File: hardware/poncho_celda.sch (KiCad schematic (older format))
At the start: 0 parts

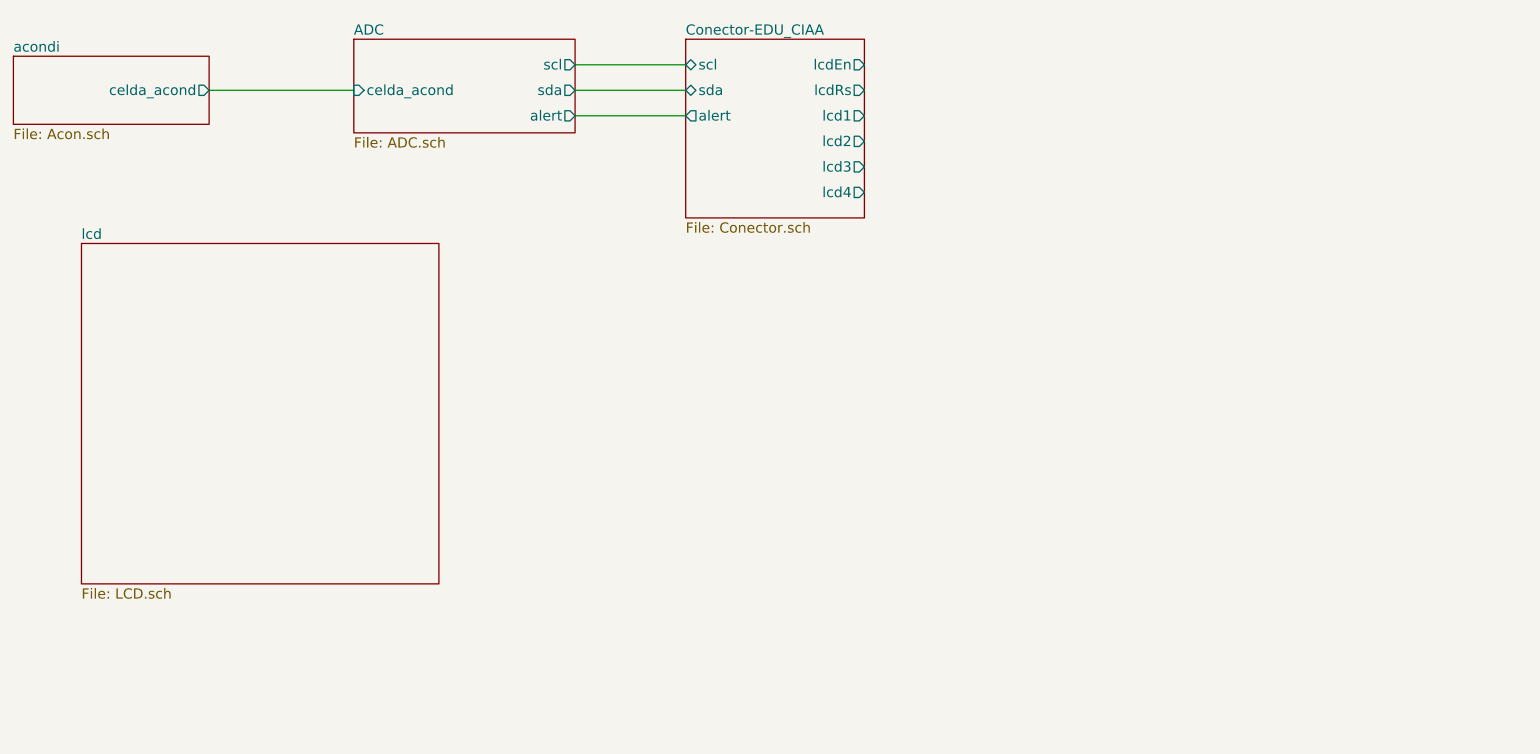
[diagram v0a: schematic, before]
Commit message: Se finalizo esquematico del cricuito.
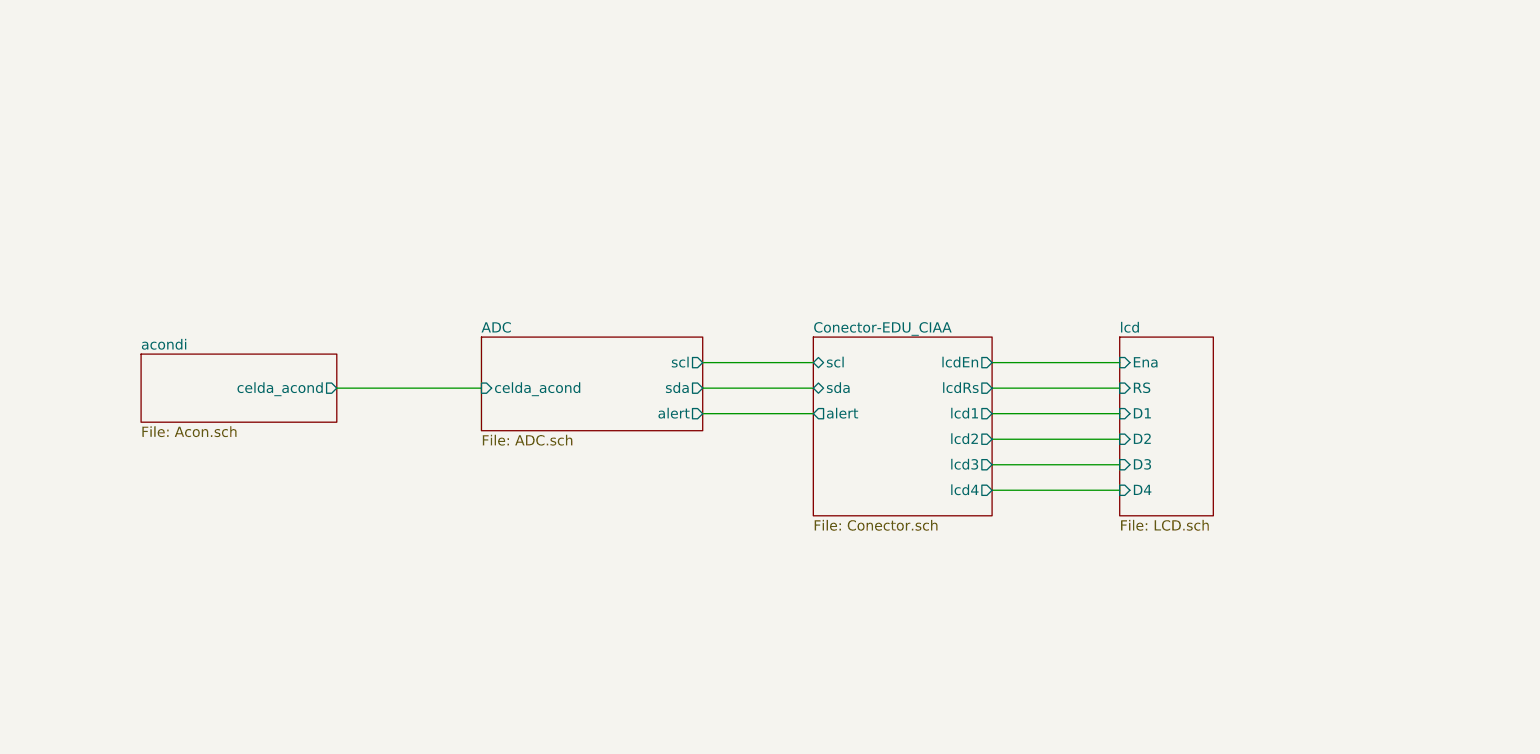
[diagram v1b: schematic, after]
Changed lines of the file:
@@
 encoding utf-8
 Sheet 1 5
-Title ""
-Date ""
+Title "Diagrama esquematico de modulos para poncho celda."
+Date "2016-07-04"
 Rev ""
-Comp ""
+Comp "Felipe Rey"
 Comment1 ""
 Comment2 ""
@@
 $EndDescr
 $Sheet
-S 3600 1500 1300 550
+S 4350 3250 1300 550
 U 57856888
 F0 "ADC" 60
 F1 "ADC.sch" 60
-F2 "celda_acond" I L 3600 1800 60
-F3 "scl" O R 4900 1650 60
-F4 "sda" O R 4900 1800 60
-F5 "alert" O R 4900 1950 60
+F2 "celda_acond" I L 4350 3550 60
+F3 "scl" O R 5650 3400 60
+F4 "sda" O R 5650 3550 60
+F5 "alert" O R 5650 3700 60
 $EndSheet
 $Sheet
-S 1600 1600 1150 400
+S 2350 3350 1150 400
 U 578568AB
 F0 "acondi" 60
 F1 "Acon.sch" 60
-F2 "celda_acond" O R 2750 1800 60
+F2 "celda_acond" O R 3500 3550 60
 $EndSheet
 $Sheet
-S 2000 2700 2100 2000
+S 8100 3250 550  1050
 U 578568C8
 F0 "lcd" 60
 F1 "LCD.sch" 60
+F2 "RS" I L 8100 3550 60
+F3 "Ena" I L 8100 3400 60
+F4 "D1" I L 8100 3700 60
+F5 "D2" I L 8100 3850 60
+F6 "D3" I L 8100 4000 60
+F7 "D4" I L 8100 4150 60
 $EndSheet
 $Sheet
-S 5550 1500 1050 1050
+S 6300 3250 1050 1050
 U 578568DA
 F0 "Conector-EDU_CIAA" 60
 F1 "Conector.sch" 60
-F2 "sda" B L 5550 1800 60
-F3 "scl" B L 5550 1650 60
-F4 "lcdEn" O R 6600 1650 60
-F5 "lcdRs" O R 6600 1800 60
-F6 "lcd1" O R 6600 1950 60
-F7 "lcd2" O R 6600 2100 60
-F8 "lcd3" O R 6600 2250 60
-F9 "lcd4" O R 6600 2400 60
-F10 "alert" O L 5550 1950 60
+F2 "sda" B L 6300 3550 60
+F3 "scl" B L 6300 3400 60
+F4 "lcdEn" O R 7350 3400 60
+F5 "lcdRs" O R 7350 3550 60
+F6 "lcd1" O R 7350 3700 60
+F7 "lcd2" O R 7350 3850 60
+F8 "lcd3" O R 7350 4000 60
+F9 "lcd4" O R 7350 4150 60
+F10 "alert" O L 6300 3700 60
 $EndSheet
 Wire Wire Line
-	2750 1800 3600 1800
+	3500 3550 4350 3550
 Wire Wire Line
-	4900 1650 5550 1650
+	5650 3400 6300 3400
 Wire Wire Line
-	4900 1800 5550 1800
+	5650 3550 6300 3550
 Wire Wire Line
-	4900 1950 5550 1950
+	5650 3700 6300 3700
+Wire Wire Line
+	7350 3400 8100 3400
+Wire Wire Line
+	8100 3550 7350 3550
+Wire Wire Line
+	8100 3700 7350 3700
+Wire Wire Line
+	8100 3850 7350 3850
+Wire Wire Line
+	8100 4000 7350 4000
+Wire Wire Line
+	8100 4150 7350 4150
 $EndSCHEMATC

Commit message: Se realizan correcciones al esquematico.
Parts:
- added DS1: LCD16X2, celda:LCD16x2, symbol LCD16X2
- added R7: 220, celda:R_1206_HandSoldering, symbol R
- added RV1: 10K, celda:POT_SMD, symbol POT
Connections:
- net Conector-EDU_CIAA/lcd1: now also DS1.11 (D4)
- net Conector-EDU_CIAA/lcd2: now also DS1.12 (D5)
- net Conector-EDU_CIAA/lcd3: now also DS1.13 (D6)
- net Conector-EDU_CIAA/lcd4: now also DS1.14 (D7)
- net Conector-EDU_CIAA/lcdEn: now also DS1.6 (E)
- net Conector-EDU_CIAA/lcdRs: now also DS1.4 (RS)
- new net: DS1.16 (LED-), R7.1
- new net: DS1.3 (VO), RV1.2
- new net +5V: DS1.15 (LED+), DS1.2 (VDD), RV1.1
- new net GND: DS1.1 (VSS), DS1.10 (D3), DS1.5 (R/W), DS1.7 (D0), DS1.8 (D1), DS1.9 (D2), R7.2, RV1.3
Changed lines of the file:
@@
 $Descr A4 11693 8268
 encoding utf-8
-Sheet 1 5
-Title "Diagrama esquematico de modulos para poncho celda."
+Sheet 1 3
+Title "Diagrama esquematico de poncho Celda."
 Date "2016-07-04"
 Rev ""
 Comp "Felipe Rey"
-Comment1 ""
-Comment2 ""
+Comment1 "Diagrama esquematico de modulos para poncho celda para el curso de Diseño de PCB del CESE."
+Comment2 "Licencia GPL V3"
 Comment3 ""
 Comment4 ""
 $EndDescr
 $Sheet
-S 4350 3250 1300 550
-U 57856888
-F0 "ADC" 60
-F1 "ADC.sch" 60
-F2 "celda_acond" I L 4350 3550 60
-F3 "scl" O R 5650 3400 60
-F4 "sda" O R 5650 3550 60
-F5 "alert" O R 5650 3700 60
+S 3000 4500 950  600
+U 578568AB
+F0 "Adqui_Celda" 60
+F1 "Acon.sch" 60
+F2 "scl" O R 3950 4600 60
+F3 "sda" O R 3950 4750 60
+F4 "alert" O R 3950 4900 60
 $EndSheet
 $Sheet
-S 2350 3350 1150 400
-U 578568AB
-F0 "acondi" 60
-F1 "Acon.sch" 60
-F2 "celda_acond" O R 3500 3550 60
-$EndSheet
-$Sheet
-S 8100 3250 550  1050
-U 578568C8
-F0 "lcd" 60
-F1 "LCD.sch" 60
-F2 "RS" I L 8100 3550 60
-F3 "Ena" I L 8100 3400 60
-F4 "D1" I L 8100 3700 60
-F5 "D2" I L 8100 3850 60
-F6 "D3" I L 8100 4000 60
-F7 "D4" I L 8100 4150 60
-$EndSheet
-$Sheet
-S 6300 3250 1050 1050
+S 4600 4450 1050 1050
 U 578568DA
 F0 "Conector-EDU_CIAA" 60
 F1 "Conector.sch" 60
-F2 "sda" B L 6300 3550 60
-F3 "scl" B L 6300 3400 60
-F4 "lcdEn" O R 7350 3400 60
-F5 "lcdRs" O R 7350 3550 60
-F6 "lcd1" O R 7350 3700 60
-F7 "lcd2" O R 7350 3850 60
-F8 "lcd3" O R 7350 4000 60
-F9 "lcd4" O R 7350 4150 60
-F10 "alert" O L 6300 3700 60
+F2 "sda" B L 4600 4750 60
+F3 "scl" B L 4600 4600 60
+F4 "lcdEn" O R 5650 4750 60
+F5 "lcdRs" O R 5650 4600 60
+F6 "lcd1" O R 5650 4900 60
+F7 "lcd2" O R 5650 5050 60
+F8 "lcd3" O R 5650 5200 60
+F9 "lcd4" O R 5650 5350 60
+F10 "alert" O L 4600 4900 60
 $EndSheet
 Wire Wire Line
-	3500 3550 4350 3550
+	3950 4600 4600 4600
 Wire Wire Line
-	5650 3400 6300 3400
+	3950 4750 4600 4750
 Wire Wire Line
-	5650 3550 6300 3550
+	3950 4900 4600 4900
+$Comp
+L LCD16X2 DS1
+U 1 1 5796E83B
+P 6600 1800
+F 0 "DS1" H 5800 2200 50  0000 C CNN
+F 1 "LCD16X2" H 7300 2200 50  0000 C CNN
+F 2 "celda:LCD16x2" H 6600 1750 50  0000 C CIN
+F 3 "" H 6600 1800 50  0000 C CNN
+	1    6600 1800
+	1    0    0    -1
+$EndComp
+$Comp
+L POT RV1
+U 1 1 5796E97F
+P 5100 2850
+F 0 "RV1" H 5100 2750 50  0000 C CNN
+F 1 "10K" H 5100 2850 50  0000 C CNN
+F 2 "celda:POT_SMD" H 5100 2850 50  0001 C CNN
+F 3 "" H 5100 2850 50  0000 C CNN
+	1    5100 2850
+	0    1    1    0
+$EndComp
+$Comp
+L +5V #PWR01
+U 1 1 5796F4BD
+P 5100 2200
+F 0 "#PWR01" H 5100 2050 50  0001 C CNN
+F 1 "+5V" H 5100 2340 50  0000 C CNN
+F 2 "" H 5100 2200 50  0000 C CNN
+F 3 "" H 5100 2200 50  0000 C CNN
+	1    5100 2200
+	1    0    0    -1
+$EndComp
+$Comp
+L +5V #PWR02
+U 1 1 5796F541
+P 7750 2150
+F 0 "#PWR02" H 7750 2000 50  0001 C CNN
+F 1 "+5V" H 7750 2290 50  0000 C CNN
+F 2 "" H 7750 2150 50  0000 C CNN
+F 3 "" H 7750 2150 50  0000 C CNN
+	1    7750 2150
+	1    0    0    -1
+$EndComp
+$Comp
+L R R7
+U 1 1 5796F5C5
+P 7350 2750
+F 0 "R7" V 7430 2750 50  0000 C CNN
+F 1 "220" V 7350 2750 50  0000 C CNN
+F 2 "celda:R_1206_HandSoldering" V 7280 2750 50  0001 C CNN
+F 3 "" H 7350 2750 50  0000 C CNN
+	1    7350 2750
+	1    0    0    -1
+$EndComp
 Wire Wire Line
-	5650 3700 6300 3700
+	7350 2300 7350 2600
 Wire Wire Line
-	7350 3400 8100 3400
+	7250 2300 7250 2450
 Wire Wire Line
-	8100 3550 7350 3550
+	7250 2450 7750 2450
 Wire Wire Line
-	8100 3700 7350 3700
+	7750 2450 7750 2150
 Wire Wire Line
-	8100 3850 7350 3850
+	5950 2300 5950 2450
 Wire Wire Line
-	8100 4000 7350 4000
+	5950 2450 5100 2450
 Wire Wire Line
-	8100 4150 7350 4150
+	5100 2200 5100 2600
+Connection ~ 5100 2450
+Wire Wire Line
+	6050 2300 6050 2850
+Wire Wire Line
+	6050 2850 5250 2850
+$Comp
+L GND #PWR03
+U 1 1 5796F813
+P 5850 3400
+F 0 "#PWR03" H 5850 3150 50  0001 C CNN
+F 1 "GND" H 5850 3250 50  0000 C CNN
+F 2 "" H 5850 3400 50  0000 C CNN
+F 3 "" H 5850 3400 50  0000 C CNN
+	1    5850 3400
+	1    0    0    -1
+$EndComp
+$Comp
+L GND #PWR04
+U 1 1 5796F899
+P 7350 3350
+F 0 "#PWR04" H 7350 3100 50  0001 C CNN
+F 1 "GND" H 7350 3200 50  0000 C CNN
+F 2 "" H 7350 3350 50  0000 C CNN
+F 3 "" H 7350 3350 50  0000 C CNN
+	1    7350 3350
+	1    0    0    -1
+$EndComp
+Wire Wire Line
+	7350 2900 7350 3350
+Wire Wire Line
+	5850 2300 5850 3400
+Wire Wire Line
+	5100 3100 5100 3300
+Wire Wire Line
+	5100 3300 5850 3300
+Connection ~ 5850 3300
+Wire Wire Line
+	6250 2300 6250 2600
+Wire Wire Line
+	5850 2600 6750 2600
+Connection ~ 5850 2600
+Wire Wire Line
+	6450 2600 6450 2300
+Connection ~ 6250 2600
+Wire Wire Line
+	6550 2600 6550 2300
+Connection ~ 6450 2600
+Wire Wire Line
+	6650 2600 6650 2300
+Connection ~ 6550 2600
+Wire Wire Line
+	6750 2600 6750 2300
+Connection ~ 6650 2600
+Wire Wire Line
+	5650 4600 6150 4600
+Wire Wire Line
+	6150 4600 6150 2300
+Wire Wire Line
+	5650 4750 6350 4750
+Wire Wire Line
+	6350 4750 6350 2300
+Wire Wire Line
+	5650 4900 6850 4900
+Wire Wire Line
+	6850 4900 6850 2300
+Wire Wire Line
+	5650 5050 6950 5050
+Wire Wire Line
+	6950 5050 6950 2300
+Wire Wire Line
+	5650 5200 7050 5200
+Wire Wire Line
+	7050 5200 7050 2300
+Wire Wire Line
+	5650 5350 7150 5350
+Wire Wire Line
+	7150 5350 7150 2300
 $EndSCHEMATC

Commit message: Correcciones en clases.
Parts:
- added F1, F2, F3: FIDUCIAL, celda:Fiducial_1mm, symbol FIDUCIAL
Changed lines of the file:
@@
 EESchema Schematic File Version 2
-LIBS:power
-LIBS:device
-LIBS:transistors
-LIBS:conn
-LIBS:linear
-LIBS:regul
-LIBS:74xx
-LIBS:cmos4000
-LIBS:adc-dac
-LIBS:memory
-LIBS:xilinx
-LIBS:microcontrollers
-LIBS:dsp
-LIBS:microchip
-LIBS:analog_switches
-LIBS:motorola
-LIBS:texas
-LIBS:intel
-LIBS:audio
-LIBS:interface
-LIBS:digital-audio
-LIBS:philips
-LIBS:display
-LIBS:cypress
-LIBS:siliconi
-LIBS:opto
-LIBS:atmel
-LIBS:contrib
-LIBS:valves
 LIBS:ej2cese
-LIBS:ADS1113IDGSR
 LIBS:poncho_celda-cache
 EELAYER 25 0
@@
 Rev ""
 Comp "Felipe Rey Hernandez"
-Comment1 "Diagrama esquematico de modulos para poncho celda para el curso de Diseño de PCB del CESE."
+Comment1 "Esquematico de modulos para poncho celda para el curso de Diseño de PCB del CESE."
 Comment2 "Licencia GPL V3"
 Comment3 ""
@@
 $EndComp
 Wire Wire Line
-	7350 2300 7350 2600
-Wire Wire Line
 	7250 2300 7250 2450
 Wire Wire Line
@@
 $EndComp
 Wire Wire Line
-	7350 2900 7350 3350
-Wire Wire Line
 	5850 2300 5850 3400
 Wire Wire Line
@@
 Wire Wire Line
 	7150 5350 7150 2300
+$Comp
+L FIDUCIAL F1
+U 1 1 5797FD72
+P 9900 2150
+F 0 "F1" H 9980 2200 40  0000 L CNN
+F 1 "FIDUCIAL" H 9900 2050 30  0001 C CNN
+F 2 "celda:Fiducial_1mm" H 9900 2200 60  0001 C CNN
+F 3 "" H 9900 2200 60  0001 C CNN
+F 4 "FIDUCIAL" H 9950 1950 60  0001 C CNN "Descripcion"
+	1    9900 2150
+	1    0    0    -1
+$EndComp
+$Comp
+L FIDUCIAL F2
+U 1 1 5797FE2C
+P 9900 2450
+F 0 "F2" H 9980 2500 40  0000 L CNN
+F 1 "FIDUCIAL" H 9900 2350 30  0001 C CNN
+F 2 "celda:Fiducial_1mm" H 9900 2500 60  0001 C CNN
+F 3 "" H 9900 2500 60  0001 C CNN
+F 4 "FIDUCIAL" H 9950 2250 60  0001 C CNN "Descripcion"
+	1    9900 2450
+	1    0    0    -1
+$EndComp
+$Comp
+L FIDUCIAL F3
+U 1 1 57980136
+P 9900 2750
+F 0 "F3" H 9980 2800 40  0000 L CNN
+F 1 "FIDUCIAL" H 9900 2650 30  0001 C CNN
+F 2 "celda:Fiducial_1mm" H 9900 2800 60  0001 C CNN
+F 3 "" H 9900 2800 60  0001 C CNN
+F 4 "FIDUCIAL" H 9950 2550 60  0001 C CNN "Descripcion"
+	1    9900 2750
+	1    0    0    -1
+$EndComp
+Wire Wire Line
+	7350 2300 7350 2500
+Wire Wire Line
+	7350 3000 7350 3350
 $EndSCHEMATC
